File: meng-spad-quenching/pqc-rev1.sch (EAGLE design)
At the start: 0 parts

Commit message: Started work on PQC, made ADCMP582 lib
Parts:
- added C1: 33p, rcl:C-EUC0805
- added C2: 100n, rcl:C-EUC0805
- added C3: (no value), rcl:CPOL-EUCT7343
- added IC1: ADCMP582, meng:ADCMP582
- added R1: 65k, rcl:R-EU_R0805
- added R2, R4: DNP, rcl:R-EU_R0805
- added R3: 1k, rcl:R-EU_R0805
- added R5: 50R, rcl:R-EU_R0805
- added X1, X2, X3, X4: SMA-142-0711-871/876, con-coax:SMA-142-0711-871/876
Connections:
- new net GND: C2.2, C3.-, IC1.GND, IC1.VTN, R2.1, R3.1, X1G1.GND, X3G1.GND, X4G1.GND
- new net N$1: IC1.VCCO
- new net N$11: R5.2, X4G1.1
- new net N$2: C1.2, IC1.VN, R2.2, R4.1
- new net N$3: C1.1, R1.1, X1G1.1
- new net N$4: IC1.HYS, R3.2
- new net N$5: C2.1, C3.+, R1.2, R5.1
- new net N$6: IC1.VEE
- new net N$7: IC1.VCCI
- new net N$9: R4.2, X3G1.1
- new net VREF: IC1.VP, IC1.VTP
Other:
- note added: "+3V3"
- note added: "+5V"
- note added: "-100mV Adj."
- note added: "-5V"
- note added: "External cap."
- note added: "Optional Bias Filter"
- note added: "Passive Quench Resistor"
- note added: "Put LVPECL to CMOS/TTL here"
- note added: "R_HYS"
- note added: "SPAD Connector"
- note added: "To scope"
- note added: "Use R2 or R4 term. if IC1 not populated"
- note added: "VA Bias"
- note added: "Zin = 50R"

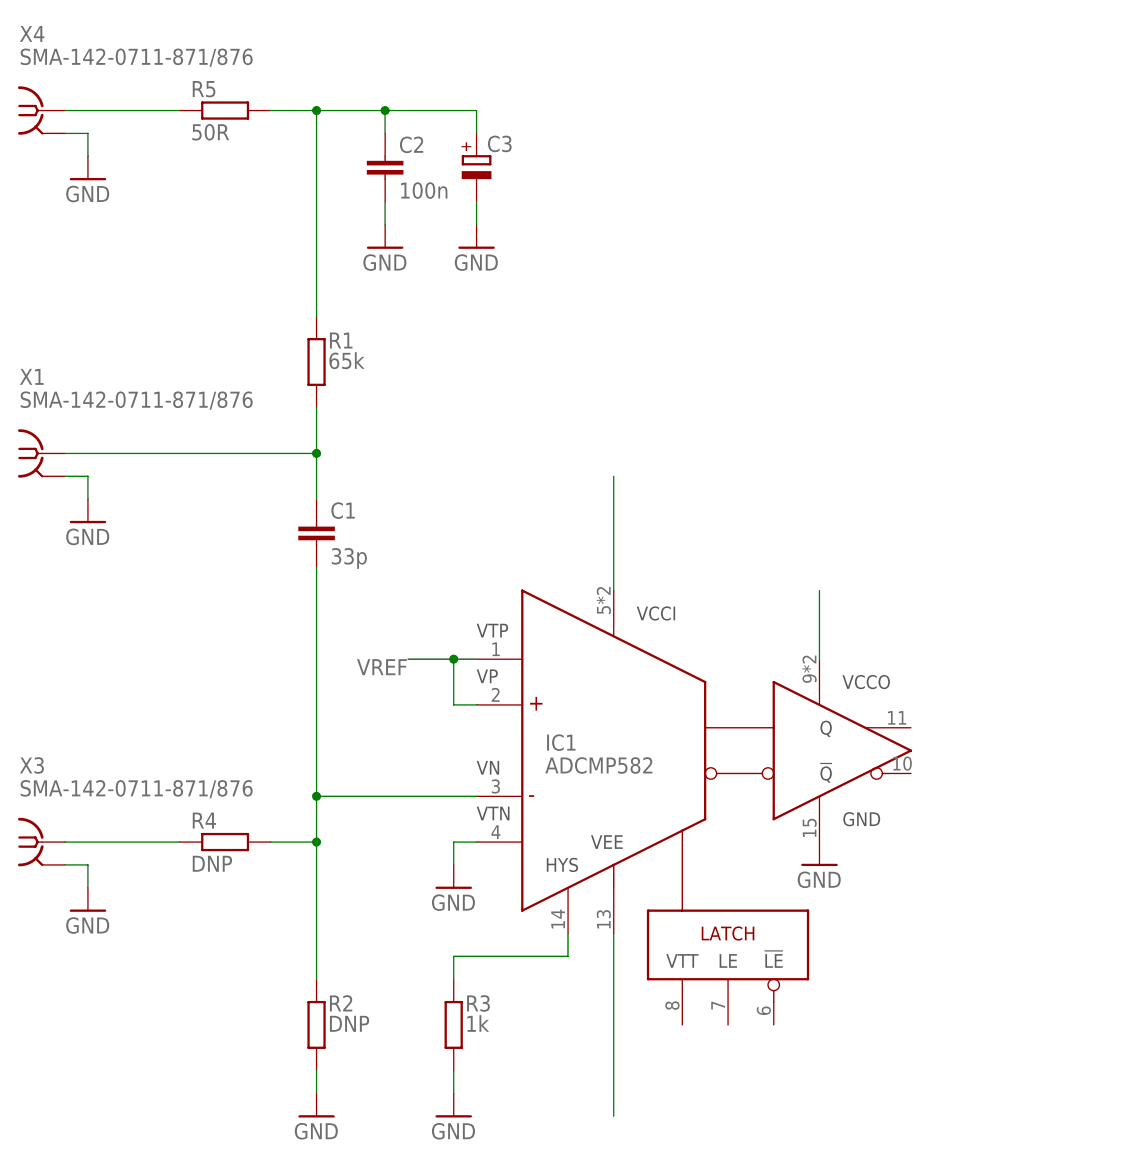
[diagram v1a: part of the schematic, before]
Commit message: Added more PQC net labels
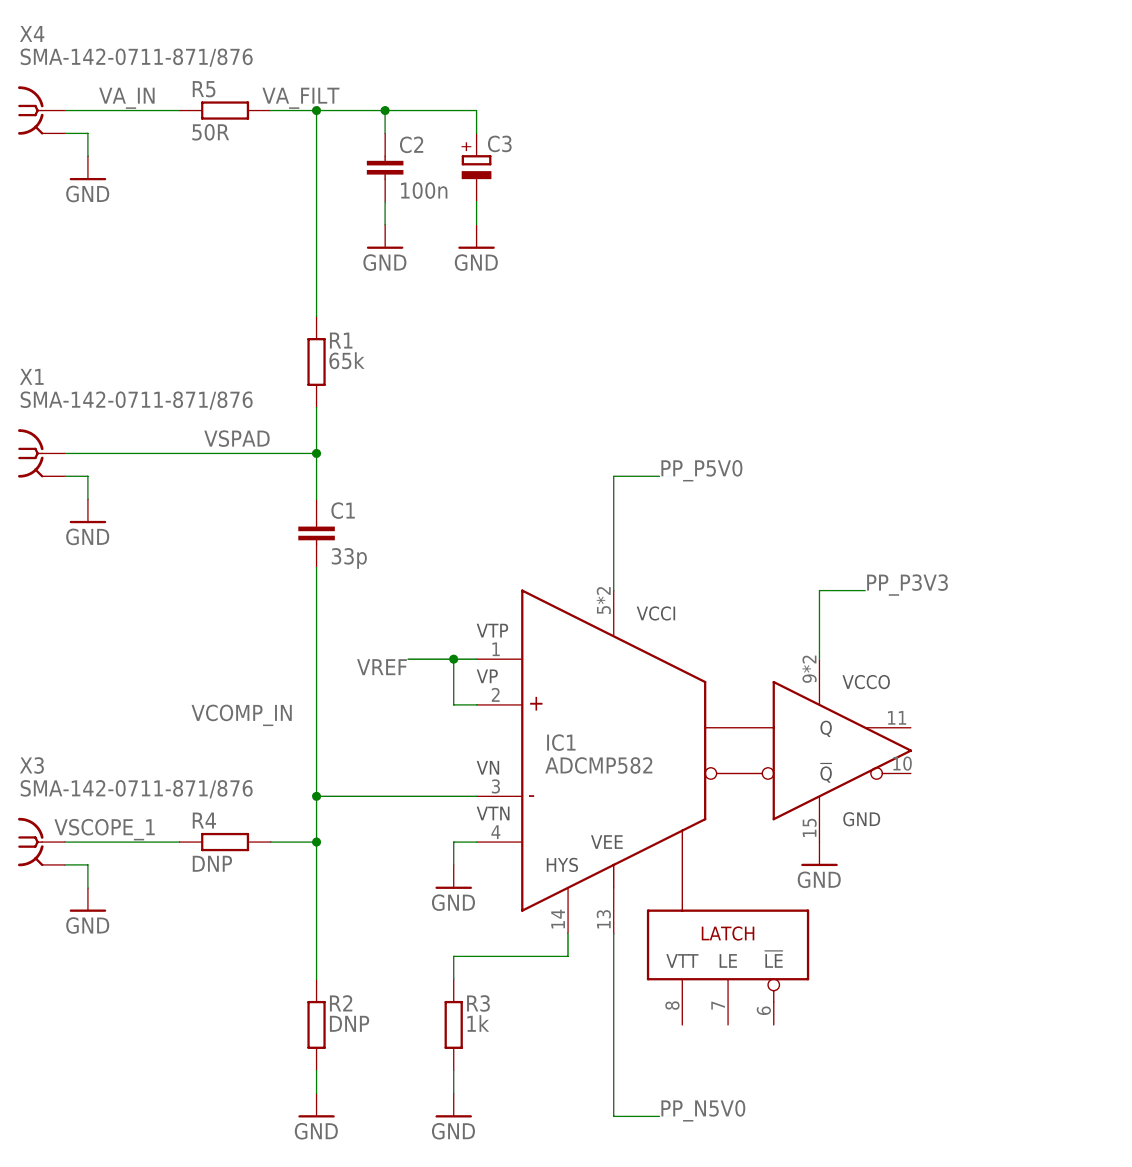
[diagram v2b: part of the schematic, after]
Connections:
- net N$1 renamed PP_P3V3
- net N$11 renamed VA_IN
- net N$2 renamed VCOMP_IN
- net N$3 renamed VSPAD
- net N$5 renamed VA_FILT
- net N$6 renamed PP_N5V0
- net N$7 renamed PP_P5V0
- net N$9 renamed VSCOPE_1
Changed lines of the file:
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@@
 </segment>
 </net>
-<net name="N$2" class="0">
+<net name="VCOMP_IN" class="0">
 <segment>
 <pinref part="IC1" gate="G$1" pin="VN"/>
@@
 <wire x1="66.04" y1="58.42" x2="71.12" y2="58.42" width="0.1524" layer="91"/>
 <junction x="71.12" y="58.42"/>
+<label x="68.58" y="73.66" size="1.778" layer="95" rot="R180"/>
 </segment>
 </net>
-<net name="N$3" class="0">
+<net name="VSPAD" class="0">
 <segment>
 <pinref part="C1" gate="G$1" pin="1"/>
@@
 <wire x1="43.18" y1="101.6" x2="71.12" y2="101.6" width="0.1524" layer="91"/>
 <junction x="71.12" y="101.6"/>
+<label x="66.04" y="104.14" size="1.778" layer="95" rot="R180"/>
 </segment>
 </net>
@@
 </segment>
 </net>
-<net name="N$5" class="0">
+<net name="VA_FILT" class="0">
 <segment>
 <pinref part="R1" gate="G$1" pin="2"/>
@@
 <wire x1="88.9" y1="139.7" x2="88.9" y2="137.16" width="0.1524" layer="91"/>
 <junction x="78.74" y="139.7"/>
+<label x="73.66" y="142.24" size="1.778" layer="95" rot="R180"/>
 </segment>
 </net>
-<net name="N$6" class="0">
+<net name="PP_N5V0" class="0">
 <segment>
 <pinref part="IC1" gate="G$1" pin="VEE"/>
 <wire x1="104.14" y1="48.26" x2="104.14" y2="27.94" width="0.1524" layer="91"/>
+<wire x1="104.14" y1="27.94" x2="109.22" y2="27.94" width="0.1524" layer="91"/>
+<label x="109.22" y="27.94" size="1.778" layer="95"/>
 </segment>
 </net>
-<net name="N$7" class="0">
+<net name="PP_P5V0" class="0">
 <segment>
 <pinref part="IC1" gate="G$1" pin="VCCI"/>
 <wire x1="104.14" y1="86.36" x2="104.14" y2="99.06" width="0.1524" layer="91"/>
+<wire x1="104.14" y1="99.06" x2="109.22" y2="99.06" width="0.1524" layer="91"/>
+<label x="109.22" y="99.06" size="1.778" layer="95"/>
 </segment>
 </net>
-<net name="N$1" class="0">
+<net name="PP_P3V3" class="0">
 <segment>
 <pinref part="IC1" gate="G$1" pin="VCCO"/>
 <wire x1="127" y1="78.74" x2="127" y2="86.36" width="0.1524" layer="91"/>
+<wire x1="127" y1="86.36" x2="132.08" y2="86.36" width="0.1524" layer="91"/>
+<label x="132.08" y="86.36" size="1.778" layer="95"/>
 </segment>
 </net>
-<net name="N$9" class="0">
+<net name="VSCOPE_1" class="0">
 <segment>
 <pinref part="X3" gate="G1" pin="1"/>
 <pinref part="R4" gate="G$1" pin="2"/>
 <wire x1="43.18" y1="58.42" x2="55.88" y2="58.42" width="0.1524" layer="91"/>
+<label x="53.34" y="60.96" size="1.778" layer="95" rot="R180"/>
 </segment>
 </net>
-<net name="N$11" class="0">
+<net name="VA_IN" class="0">
 <segment>
 <pinref part="X4" gate="G1" pin="1"/>
 <pinref part="R5" gate="G$1" pin="2"/>
 <wire x1="43.18" y1="139.7" x2="55.88" y2="139.7" width="0.1524" layer="91"/>
+<label x="53.34" y="142.24" size="1.778" layer="95" rot="R180"/>
 </segment>
 </net>

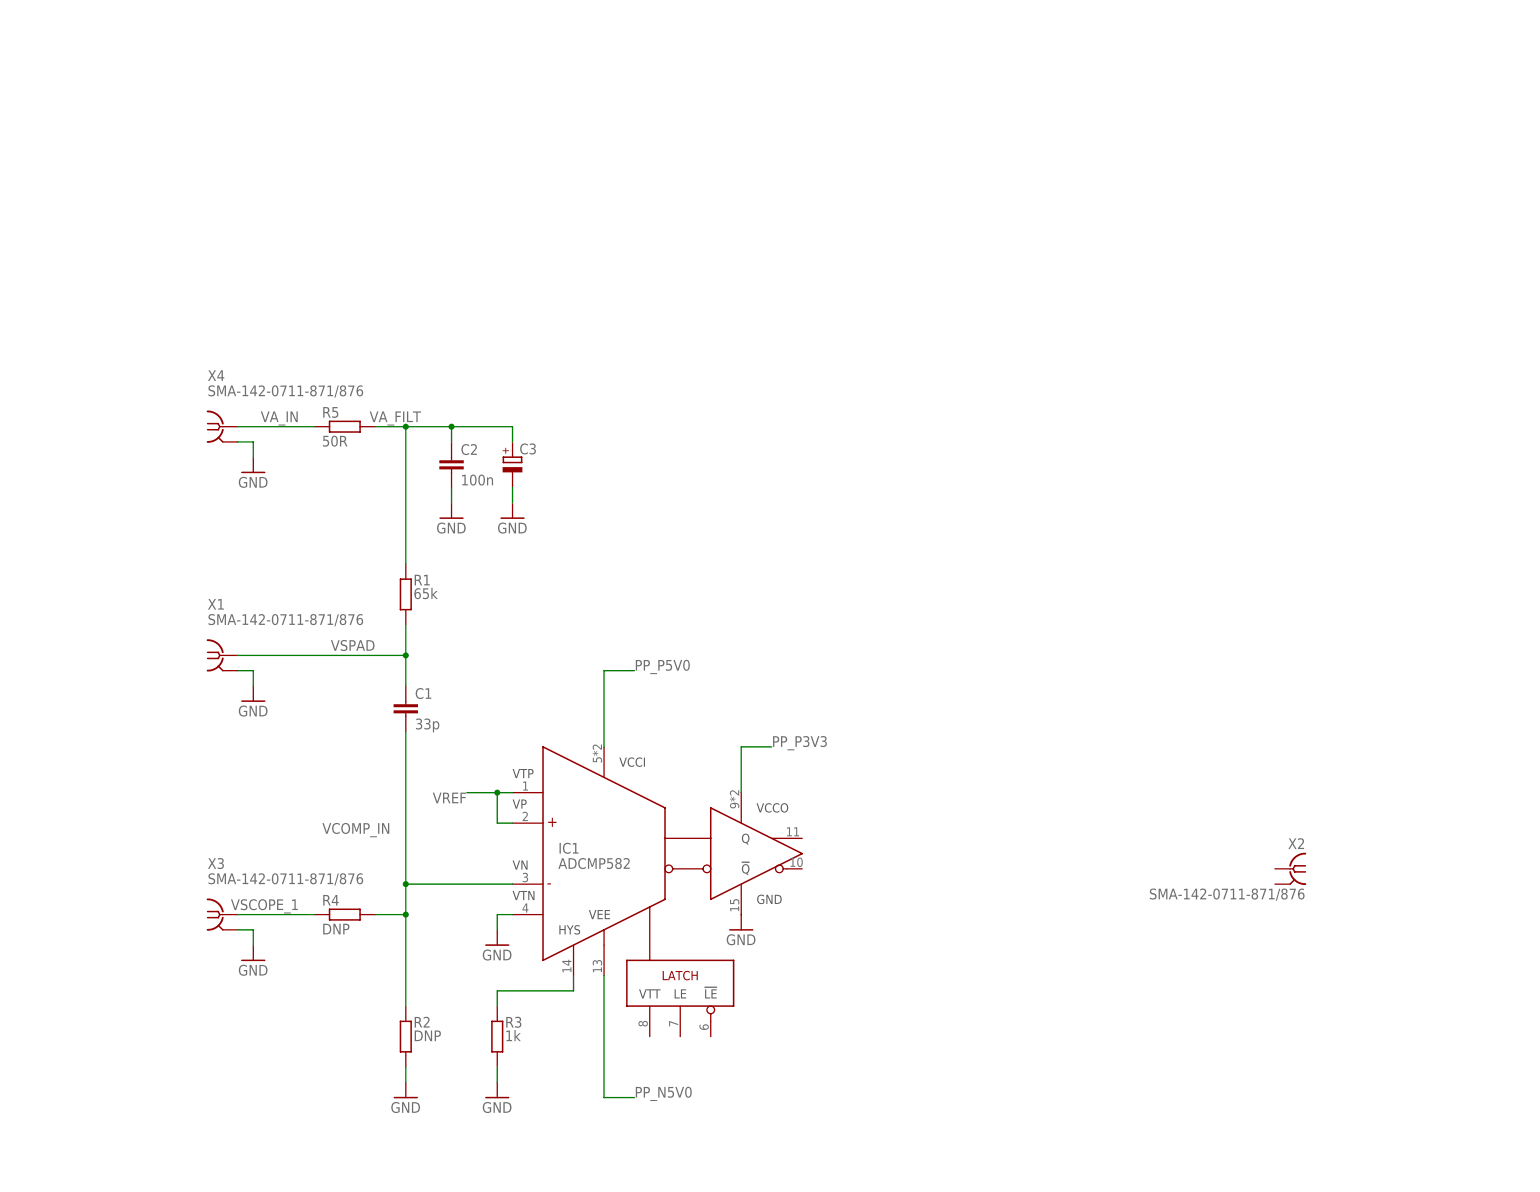
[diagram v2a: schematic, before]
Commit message: Completed pqc-rev1 layout, exported gerbers
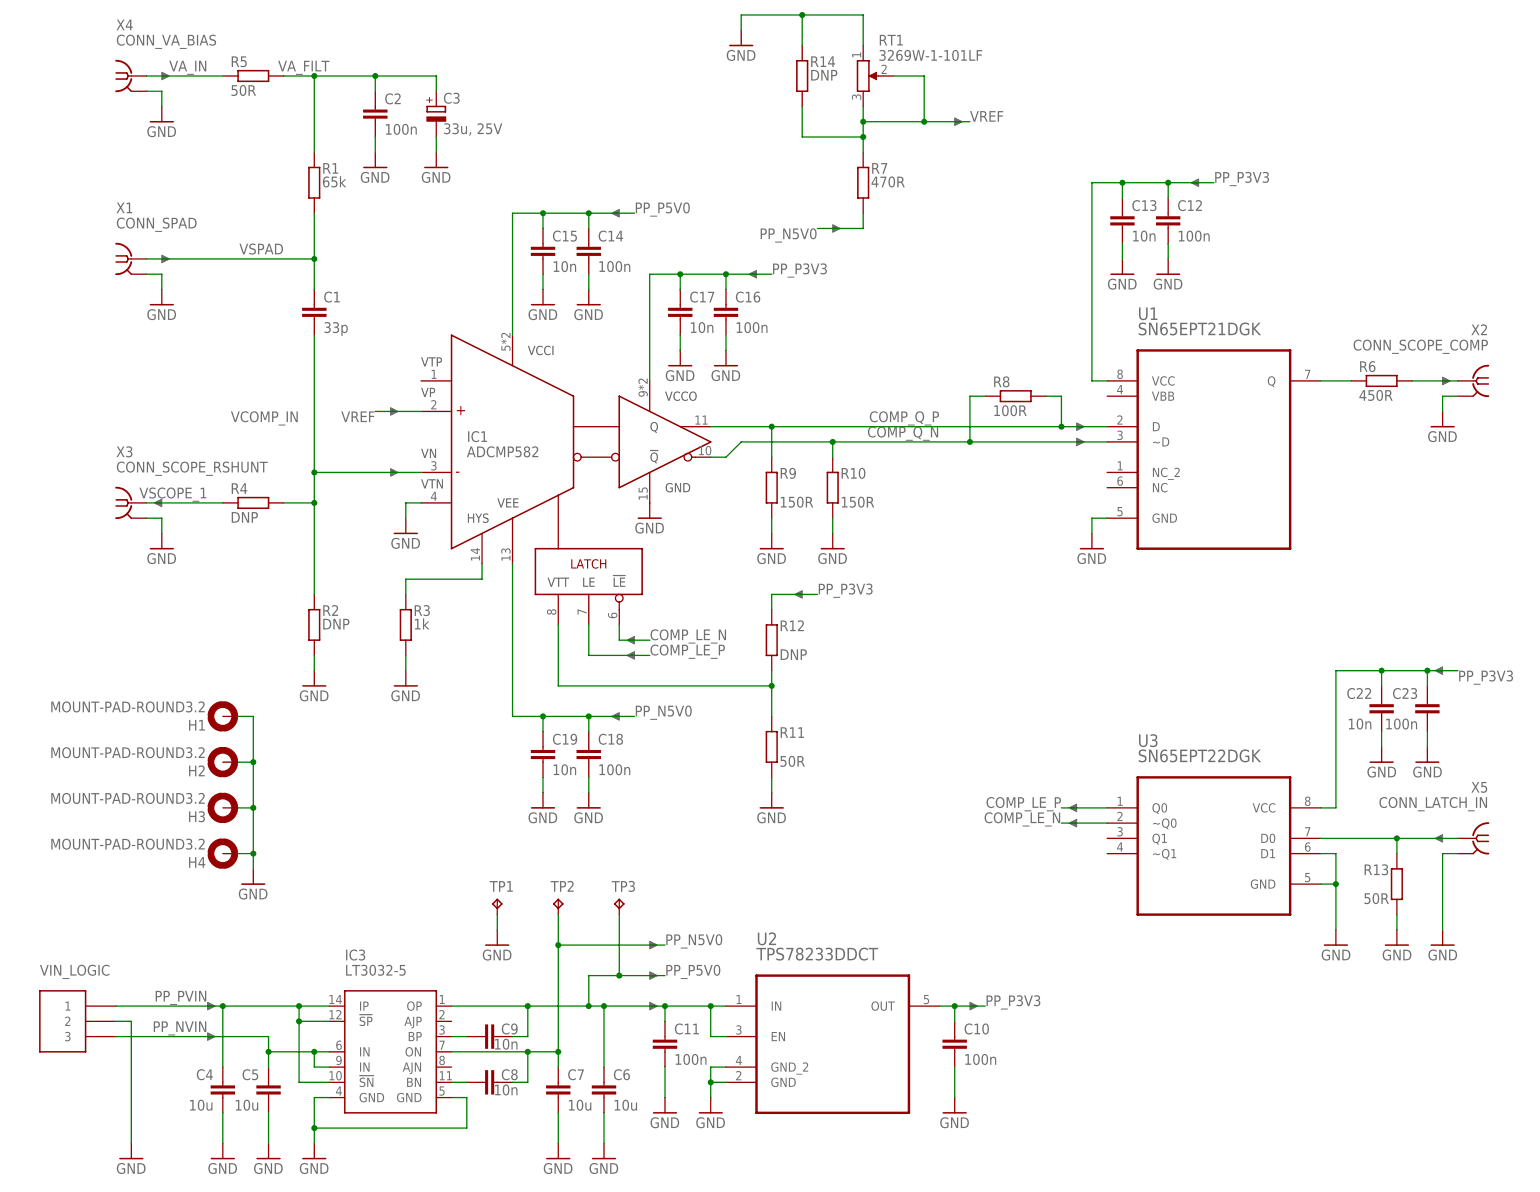
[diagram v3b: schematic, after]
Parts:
- added C10, C11, C12, C14, C16, C18, C23: 100n, rcl:C-EUC0603
- added C13, C15, C17, C19, C22, C8, C9: 10n, rcl:C-EUC0603
- added C4, C5, C6, C7: 10u, rcl:C-EUC1206
- added H1, H2, H3, H4: MOUNT-PAD-ROUND3.2, holes:MOUNT-PAD-ROUND3.2
- added IC3: LT3032-5, meng:LT3032
- added J1: VIN_LOGIC, Kramnik's Library:CONN_MOLEX_3PIN_MINI-FIT_JR
- added R10, R9: 150R, rcl:R-EU_R0603
- added R11, R13: 50R, rcl:R-EU_R0603
- added R12: DNP, rcl:R-EU_R0603
- added R14: DNP, rcl:R-EU_R0805
- added R6: 450R, rcl:R-EU_R0805
- added R7: 470R, rcl:R-EU_R0805
- added R8: 100R, rcl:R-EU_R0603
- added RT1: 3269W-1-101LF, meng:BOURNS_3269WX
- added TP1, TP2, TP3: TPTP20R, testpad:TPTP20R
- added U1: SN65EPT21DGK, Texas Instruments_By_element14_Batch_1:SN65EPT21DGK
- added U2: TPS78233DDCT, Texas Instruments_By_element14_Batch_1 (2):TPS78233DDCT
- added U3: SN65EPT22DGK, Texas Instruments_By_element14_Batch_1:SN65EPT22DGK
- added X5: CONN_LATCH_IN, con-coax:SMA-142-0711-871/876
- C3: value (none) -> 33u, 25V
- R2, R4: device rcl:R-EU_R0805 -> rcl:R-EU_R0603
- X1: value SMA-142-0711-871/876 -> CONN_SPAD
- X2: value SMA-142-0711-871/876 -> CONN_SCOPE_COMP
- X3: value SMA-142-0711-871/876 -> CONN_SCOPE_RSHUNT
- X4: value SMA-142-0711-871/876 -> CONN_VA_BIAS
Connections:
- new net COMP_LE_N: IC1.!LE, U3.~Q0
- new net COMP_LE_P: IC1.LE, U3.Q0
- new net COMP_Q_N: IC1.!Q, R10.1, R8.1, U1.~D
- new net COMP_Q_P: IC1.Q, R8.2, R9.1, U1.D
- new net N$1: R6.2, U1.Q
- new net N$10: R13.1, U3.D0, X5G1.1
- new net N$2: R6.1, X2G1.1
- new net N$6: IC1.VTT, R11.1, R12.2
- new net N$8: C9.1, IC3.BP
- new net N$9: C8.1, IC3.BN
- new net PP_NVIN: C5.1, IC3.IN, IC3.IN@1, J1.3
- new net PP_PVIN: C4.1, IC3.!SN, IC3.!SP, IC3.IP, J1.1
- net GND: now also C10.2, C11.2, C12.2, C13.2, C14.2, C15.2, C16.2, C17.2, C18.2, C19.2, C22.2, C23.2, C4.2, C5.2, C6.2, C7.2, H1.MOUNT, H2.MOUNT, H3.MOUNT, H4.MOUNT, IC3.GND, IC3.GND@1, J1.2, R10.2, R11.2, R13.2, R14.2, R9.2, RT1.1, TP1.TP, U1.GND, U2.GND, U2.GND_2, U3.D1, U3.GND, X2G1.GND, X5G1.GND
- net PP_N5V0: now also C18.1, C19.1, C7.1, C8.2, IC3.ON, R7.1, TP2.TP
- net PP_P3V3: now also C10.1, C12.1, C13.1, C16.1, C17.1, C22.1, C23.1, R12.1, U1.VCC, U2.OUT, U3.VCC
- net PP_P5V0: now also C11.1, C14.1, C15.1, C6.1, C9.2, IC3.OP, TP3.TP, U2.EN, U2.IN
- net VREF: now also R14.1, R7.2, RT1.2, RT1.3; no longer IC1.VTP
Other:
- note added: "+ 3V3 LDO"
- note added: "+/- 5V LDO"
- note added: "100R"
- note added: "AJP and AJN are NC in fixed version"
- note added: "D, !D! have symmetric 50k pulls"
- note added: "ECL Termination Reference: http://www.edn.com/Home/PrintView?contentItemId=4427861"
- note added: "From sig. gen."
- note added: "LVPECL to CMOS/TTL"
- note added: "MOLEX_0039302031"
- note added: "Panasonic EEF-CX1E330R"
- note added: "Pi Termination Network"
- note added: "T Termination Network"
- note added: "VBB is at 2V bias"
- note added: "Zdiff = 100R"
- note removed: "+3V3"
- note removed: "+5V"
- note removed: "-5V"
- note removed: "Put LVPECL to CMOS/TTL here"
- moved on the sheet: C1, C2, C3, IC1, R1, R2, R3, R4, R5, X1, X2, X3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
